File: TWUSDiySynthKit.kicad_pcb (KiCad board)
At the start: 2 copper layers, 198.4 x 65 mm, 53 parts, among them J1 Conn_02x02_Counter_Clockwise, J10 Conn_01x03_Socket, J2 Conn_01x02, J3 Conn_01x07_Pin, J4 Conn_01x07_Pin, J5 Raspberry_Pi_2x20_PTH, J6 Conn_01x04_Socket, J7 Conn_01x04_Socket, J8 Conn_01x04_Socket, J9 Conn_01x03_Socket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

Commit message: Added p2.54mm dupont headers as alternative for Stemma JST connectors
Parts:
- added J11: Conn_01x03_Socket, Connector_PinSocket_2.54mm:PinSocket_1x03_P2.54mm_Vertical, F.Cu at (69.8, 59.3)
- added J12: Conn_01x03_Socket, Connector_PinSocket_2.54mm:PinSocket_1x03_P2.54mm_Vertical, F.Cu at (69.8, 49.5)
- added J14: Conn_01x04_Socket, Connector_PinSocket_2.54mm:PinSocket_1x04_P2.54mm_Vertical, F.Cu at (72.9, 29.3)
- moved R9 2.00 mm to (69.8, 33.0)
- moved R8 1.20 mm to (75.8, 30.7)
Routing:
- net GND: track 617.6 -> 731.5 mm, vias 778 -> 784
- net +3.3V: track 262.9 -> 249.0 mm
- net Net-(A1-GPIO21): track 118.6 -> 120.6 mm
- net Net-(A1-GPIO2): track 143.0 -> 141.0 mm
- net Net-(A1-GPIO22): track 239.1 -> 239.9 mm

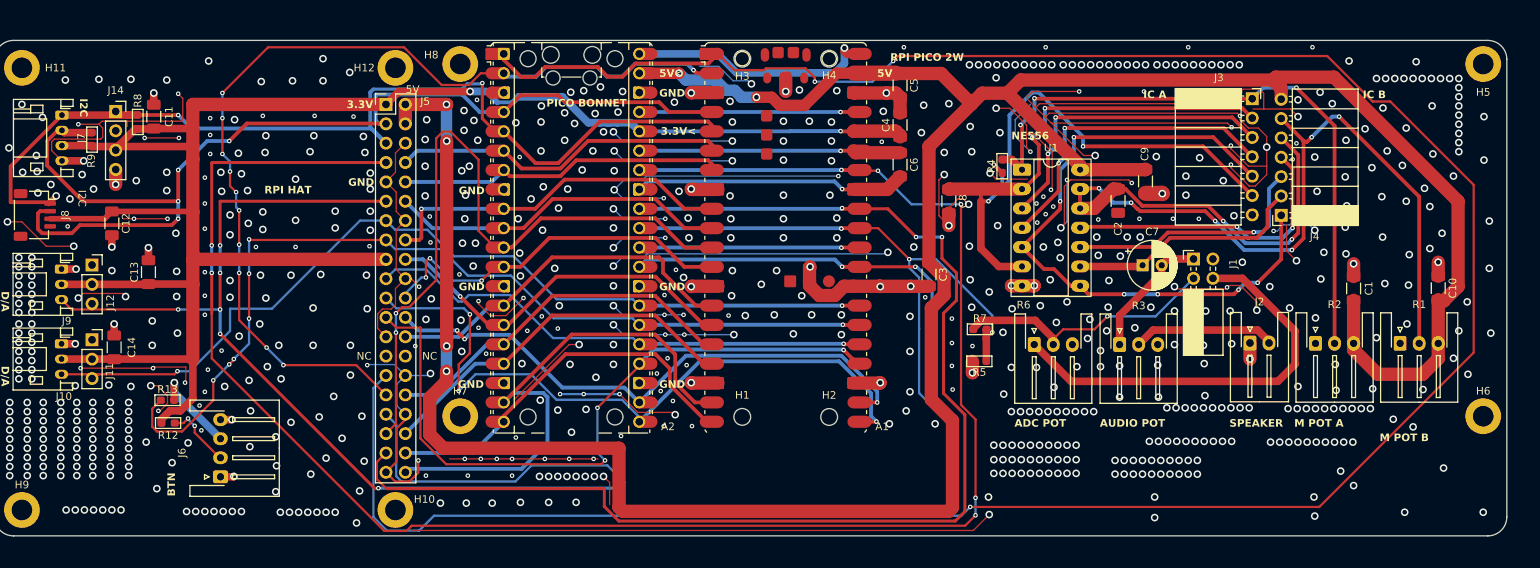
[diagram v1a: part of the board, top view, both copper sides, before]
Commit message: Added further guarding traces to reduce EMI, optimised vias etc. etc.
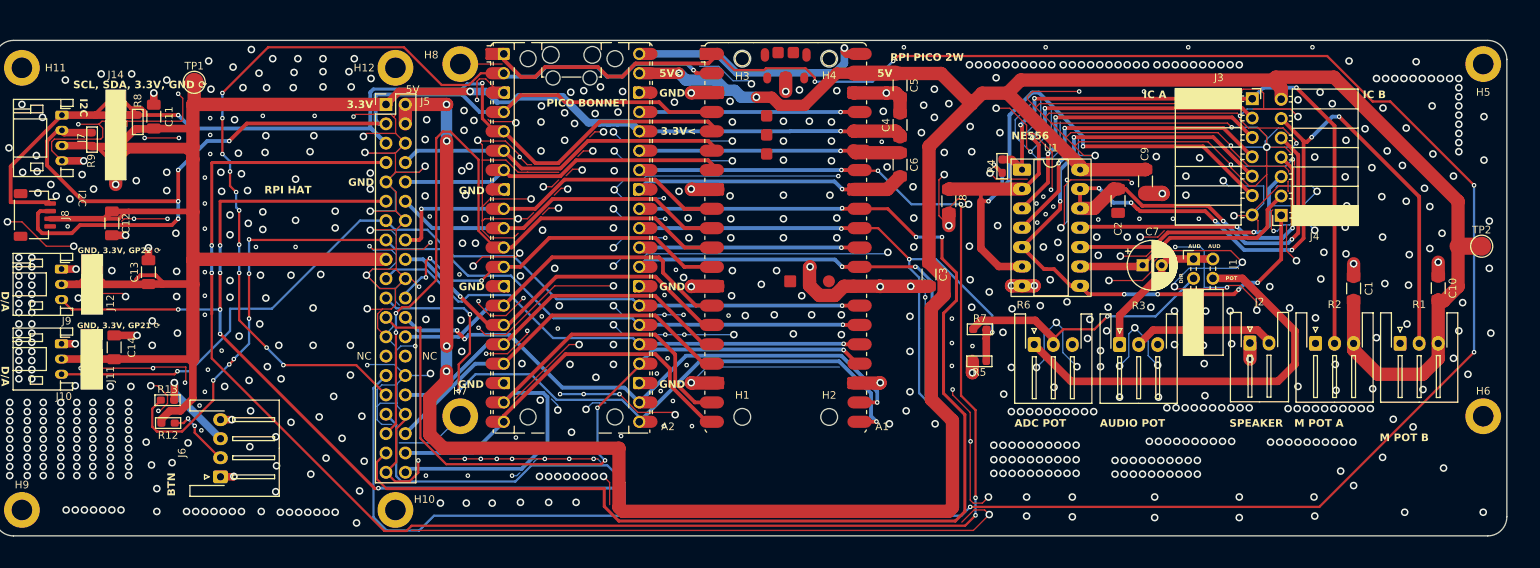
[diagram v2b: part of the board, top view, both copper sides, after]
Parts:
- added TP1: TestPoint, TestPoint:TestPoint_Pad_D2.5mm, F.Cu at (83.2, 25.5)
- added TP2: TestPoint, TestPoint:TestPoint_Pad_D2.5mm, F.Cu at (252.1, 47.0)
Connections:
- J1 pad 3: unconnected-(J1-Pin_3-Pad3) -> Net-(J1-Pin_1)
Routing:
- net GND: track 731.5 -> 1284.8 mm, vias 784 -> 813
- net +3.3V: track 249.0 -> 280.0 mm
- net Net-(A1-GPIO3): track 128.4 -> 136.7 mm
- net 5V: track 376.2 -> 379.3 mm
- net Net-(J1-Pin_1): track 17.2 -> 19.7 mm
- net Net-(A1-GPIO0): vias 3 -> 5
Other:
- board text added: "AUD"
- board text added: "DIR"
- board text added: "GND, 3.3V, GP21 ⟳"
- board text added: "GND, 3.3V, GP22 ⟳"
- board text added: "POT"
- board text added: "SCL, SDA, 3.3V, GND ⟳"
